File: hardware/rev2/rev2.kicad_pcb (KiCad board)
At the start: 2 copper layers, 24 parts, among them J1 Conn_01x09_Female, J2 RFM9X_header, J3 Conn_02x03_Odd_Even, U2 MPL3115A2, U3 Teensy3.6, U5 ADXL345BCCZ, U7 TPS2113ADRBR

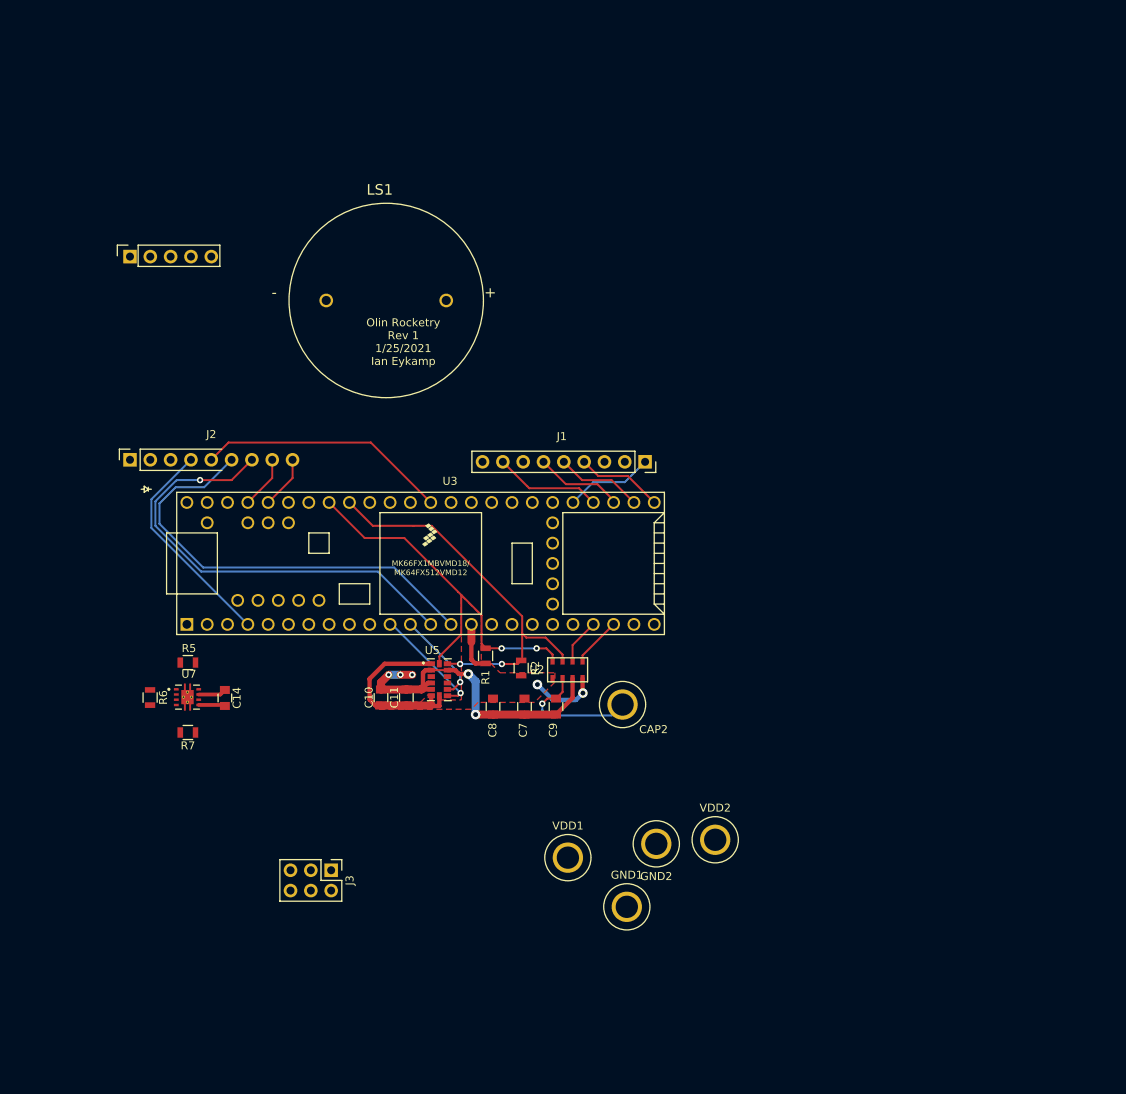
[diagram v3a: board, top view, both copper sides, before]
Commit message: add LEDs to footprint
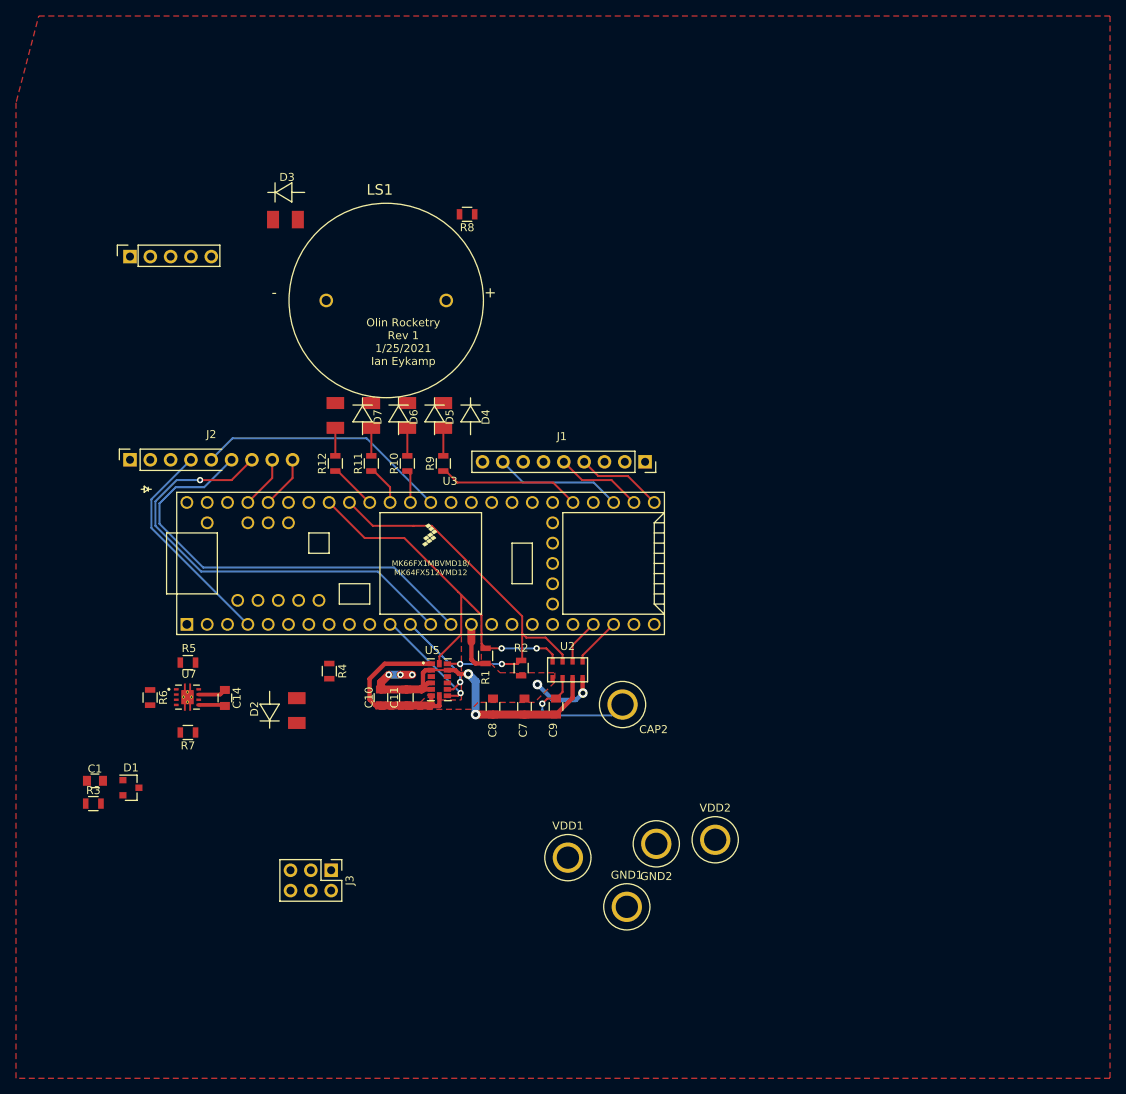
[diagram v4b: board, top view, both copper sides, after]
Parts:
- added C1: C_10uF, footprints:C_0805_OEM, F.Cu at (103.9, 122.2)
- added D1: D_Zener, Package_TO_SOT_SMD:SOT-23, F.Cu at (108.4, 123.0)
- added D2: LED, KingbrightLED:AA3528LSECKT-J4, F.Cu at (129.2, 113.4)
- added D3: LED, KingbrightLED:AA3528LSECKT-J4, F.Cu at (127.8, 52.0)
- added D4: LED, KingbrightLED:AA3528LSECKT-J4, F.Cu at (147.5, 76.5)
- added D5: LED, KingbrightLED:AA3528LSECKT-J4, F.Cu at (143.0, 76.5)
- added D6: LED, KingbrightLED:AA3528LSECKT-J4, F.Cu at (138.5, 76.5)
- added D7: LED, KingbrightLED:AA3528LSECKT-J4, F.Cu at (134.0, 76.5)
- added R10: R_750, footprints:R_0805_OEM, F.Cu at (143.0, 82.5)
- added R11: R_750, footprints:R_0805_OEM, F.Cu at (138.5, 82.5)
- added R12: R_750, footprints:R_0805_OEM, F.Cu at (134.0, 82.5)
- added R3: R_20, footprints:R_0805_OEM, F.Cu at (103.7, 125.0)
- added R4: R_750, footprints:R_0805_OEM, F.Cu at (133.2, 108.5)
- added R8: R_750, footprints:R_0805_OEM, F.Cu at (150.5, 51.4)
- added R9: R_750, footprints:R_0805_OEM, F.Cu at (147.5, 82.5)
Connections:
- C14 pad 1: BMS_to_Teensy -> BMS_TO_ZENER
- U3 pad 32: FIX -> ENABLE_GPS
- U3 pad 33: ENABLE_GPS -> BUZZER
- U3 pad 34: PPS -> LED1
- U3 pad 35: BUZZER -> Net-(U3-Pad35)
- U3 pad 39: Net-(U3-Pad39) -> GND
- U3 pad 42: Net-(U3-Pad42) -> LED2
- U3 pad 43: Net-(U3-Pad43) -> LED3
- U3 pad 44: Net-(U3-Pad44) -> LED4
- U7 pad 7: BMS_to_Teensy -> BMS_TO_ZENER
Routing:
- net LED1: track 0.00 -> 17.8 mm
- net PPS: track 11.1 -> 0.00 mm
- net FIX: track 11.0 -> 0.00 mm
- net LED4: track 0.00 -> 5.93 mm
- net LED3: track 0.00 -> 5.09 mm
- net LED2: track 0.00 -> 4.08 mm
- net BMS_to_Teensy: track 3.51 -> 0.00 mm
- net BMS_TO_ZENER: track 0.00 -> 3.51 mm
- net Net-(D7-Pad2): track 0.00 -> 3.50 mm
- net Net-(D6-Pad2): track 0.00 -> 3.50 mm
- net Net-(D5-Pad2): track 0.00 -> 3.50 mm
- net Net-(D4-Pad2): track 0.00 -> 3.50 mm
- net ENABLE_GPS: track 13.4 -> 16.0 mm
- added copper zone on F.Cu, net GND

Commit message: wip
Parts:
- moved C1 36.5 mm to (109.3, 86.1)
- moved J3 10.7 mm to (129.5, 123.4)
- moved R6 9.70 mm to (120.4, 110.1), turned to 180 degrees
- moved C14 8.44 mm to (115.7, 119.0), turned to 180 degrees
- moved D1 7.41 mm to (107.7, 130.4)
- moved R3 7.41 mm to (103.0, 132.4)
- moved R7 6.07 mm to (116.1, 110.1), turned to 0 degrees
- moved U7 5.19 mm to (120.0, 114.4), turned to 270 degrees
- moved R5 4.88 mm to (120.4, 107.4)
- moved D2 4.07 mm to (133.2, 113.5)
- moved R8 2.54 mm to (153.0, 51.4)
- moved D3 1.59 mm to (126.3, 51.4)
- moved LS1 1.58 mm to (140.3, 60.6)
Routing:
- net Net-(R5-Pad1): track 0.00 -> 5.67 mm
- net GND: track 49.4 -> 53.8 mm
- net 3.3V_TEENSY: track 37.8 -> 41.8 mm
- net Net-(R7-Pad2): track 0.00 -> 3.67 mm
- net BMS_TO_ZENER: track 3.51 -> 0.00 mm

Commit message: wip
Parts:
- moved D1 27.0 mm to (111.2, 103.6), turned to 180 degrees
- moved R3 25.2 mm to (110.1, 108.3), turned to 270 degrees
- moved C14 11.0 mm to (112.8, 108.3), turned to 90 degrees
- moved J3 8.62 mm to (130.8, 114.9)
- moved R7 6.89 mm to (122.0, 106.4), turned to 180 degrees
- moved U7 5.92 mm to (117.5, 109.0), turned to 180 degrees
- moved R5 4.53 mm to (124.5, 109.4), turned to 270 degrees
- moved R4 2.67 mm to (135.6, 107.1)
- moved D2 2.67 mm to (135.6, 112.2)
- moved R6 1.58 mm to (121.8, 109.4), turned to 90 degrees
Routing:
- net BMS_to_Teensy: track 0.00 -> 22.0 mm
- net 3.3VBMS_Backup: track 0.00 -> 21.1 mm, vias 0 -> 1
- net 3.3VBMS: track 0.00 -> 16.5 mm
- net BMS_TO_ZENER: track 0.00 -> 6.08 mm
- net Net-(R7-Pad2): track 3.67 -> 2.90 mm

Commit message: wip
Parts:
- moved C9 2.52 mm to (159.1, 112.9)
- moved C7 1.26 mm to (156.4, 112.9)
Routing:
- net GND: track 53.8 -> 40.5 mm
- net Net-(C9-Pad1): track 16.5 -> 4.51 mm, vias 1 -> 0
- net 3.3V_TEENSY: track 41.8 -> 49.1 mm, vias 2 -> 3

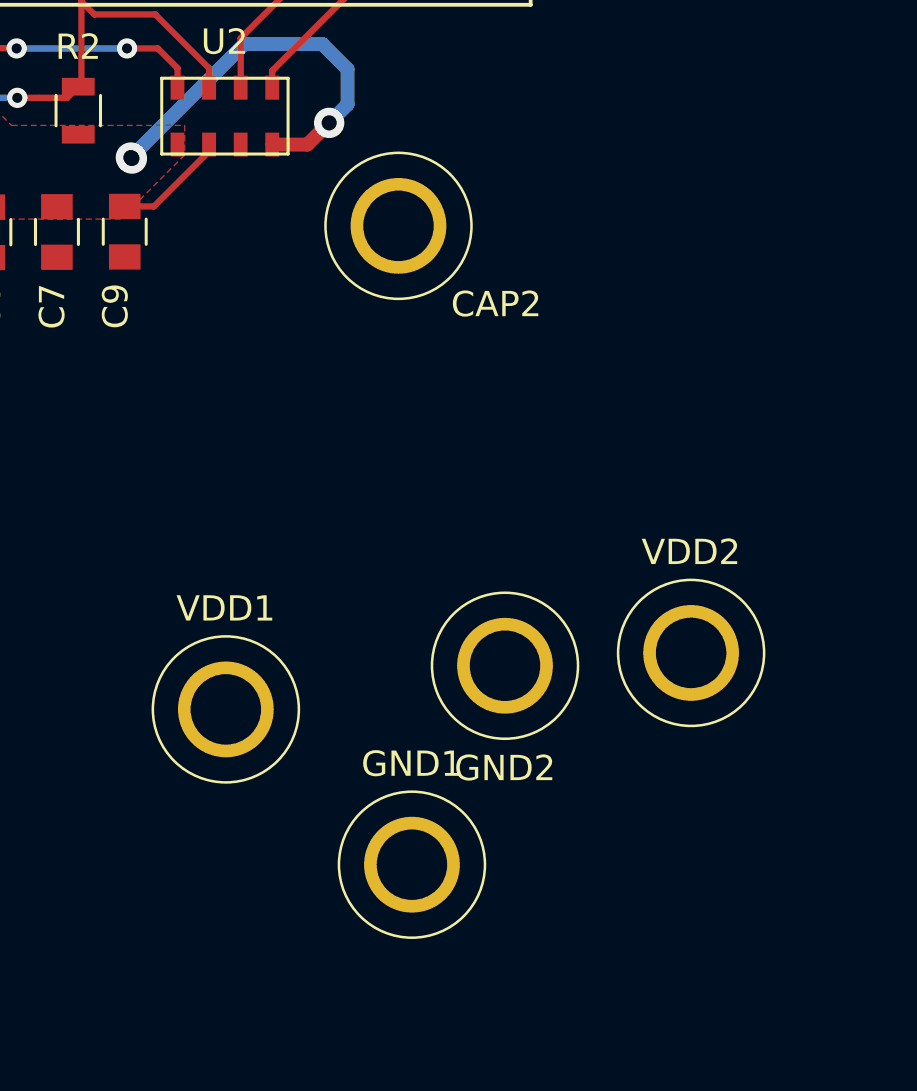
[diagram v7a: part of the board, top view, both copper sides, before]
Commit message: remove test points from layout
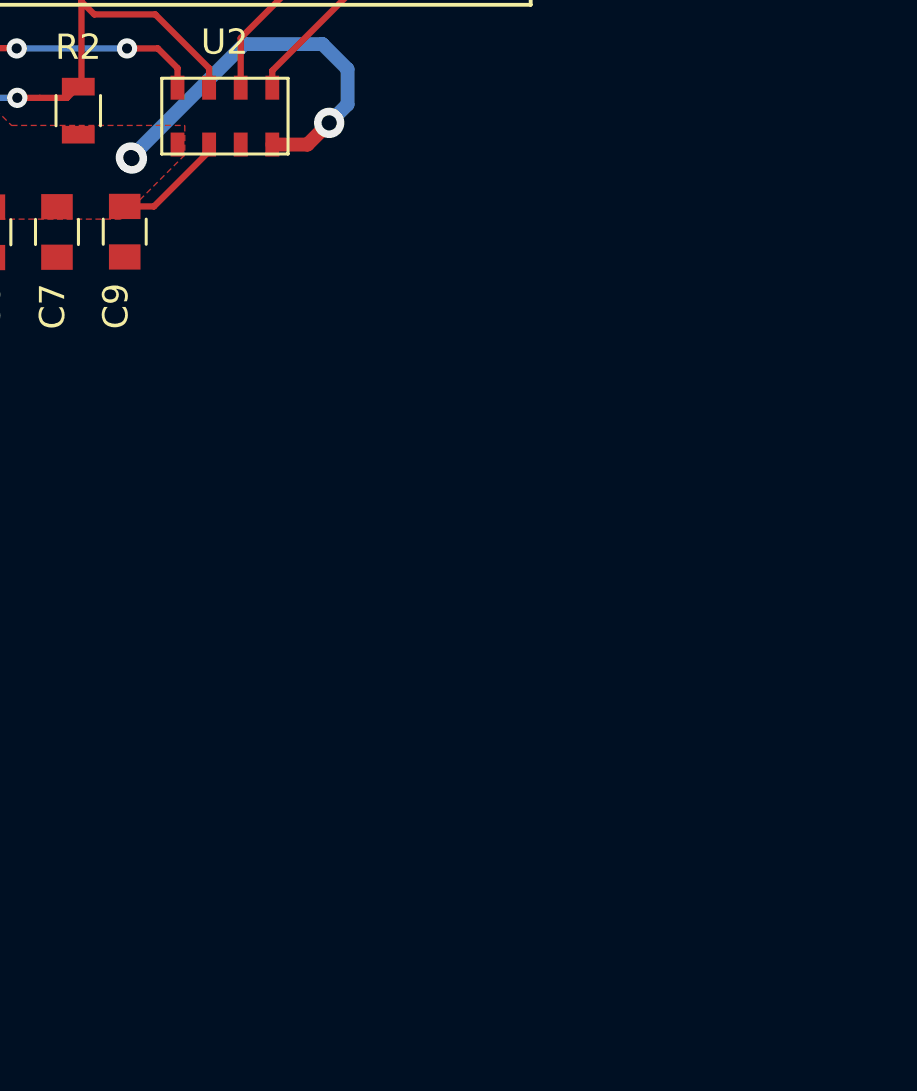
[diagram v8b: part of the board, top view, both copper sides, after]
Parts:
- removed CAP2, GND1, GND2, VDD1, VDD2: TestPoint, footprints:Test-Point-Pin_Drill2.79mm
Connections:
- D1 pad 2: Net-(D1-Pad2) -> (no net)
- J1 pad 1: PPS -> (no net)
- J1 pad 6: FIX -> (no net)
- J1 pad 7: Net-(J1-Pad7) -> (no net)
- J1 pad 9: Net-(J1-Pad9) -> (no net)
- J2 pad 10: Net-(J2-Pad10) -> (no net)
- J2 pad 11: Net-(J2-Pad11) -> (no net)
- J2 pad 12: Net-(J2-Pad12) -> (no net)
- J2 pad 13: Net-(J2-Pad13) -> (no net)
- J2 pad 14: Net-(J2-Pad14) -> (no net)
- J2 pad 7: Net-(J2-Pad7) -> (no net)
- J3 pad 6: Net-(J3-Pad6) -> (no net)
- U3 pad 10: Net-(U3-Pad10) -> (no net)
- U3 pad 16: Net-(U3-Pad16) -> (no net)
- U3 pad 17: Net-(U3-Pad17) -> (no net)
- U3 pad 18: Net-(U3-Pad18) -> (no net)
- U3 pad 19: Net-(U3-Pad19) -> (no net)
- U3 pad 2: Net-(U3-Pad2) -> (no net)
- U3 pad 20: Net-(U3-Pad20) -> (no net)
- U3 pad 23: Net-(U3-Pad23) -> (no net)
- U3 pad 24: Net-(U3-Pad24) -> (no net)
- U3 pad 25: Net-(U3-Pad25) -> (no net)
- U3 pad 26: Net-(U3-Pad26) -> (no net)
- U3 pad 27: Net-(U3-Pad27) -> (no net)
- U3 pad 28: Net-(U3-Pad28) -> (no net)
- U3 pad 29: Net-(U3-Pad29) -> (no net)
- U3 pad 3: Net-(U3-Pad3) -> (no net)
- U3 pad 35: Net-(U3-Pad35) -> (no net)
- U3 pad 36: Net-(U3-Pad36) -> (no net)
- U3 pad 37: Net-(U3-Pad37) -> (no net)
- U3 pad 38: Net-(U3-Pad38) -> (no net)
- U3 pad 40: Net-(U3-Pad40) -> (no net)
- U3 pad 47: Net-(U3-Pad47) -> (no net)
- U3 pad 48: Net-(U3-Pad48) -> (no net)
- U3 pad 5: Net-(U3-Pad5) -> (no net)
- U3 pad 51: Net-(U3-Pad51) -> (no net)
- U3 pad 52: Net-(U3-Pad52) -> (no net)
- U3 pad 54: Net-(U3-Pad54) -> (no net)
- U3 pad 55: Net-(U3-Pad55) -> (no net)
- U3 pad 56: Net-(U3-Pad56) -> (no net)
- U3 pad 57: Net-(U3-Pad57) -> (no net)
- U3 pad 6: Net-(U3-Pad6) -> (no net)
- U3 pad 9: Net-(U3-Pad9) -> (no net)
- U5 pad 10: Net-(U5-Pad10) -> (no net)
- U7 pad 1: Net-(U7-Pad1) -> (no net)
